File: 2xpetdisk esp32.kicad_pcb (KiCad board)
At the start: 2 copper layers, 75 x 100 mm, 252 parts, among them J1 Conn_01x08, J3 Micro_SD_Card_Det2, J31 PET_IEEE_M, J4 PET_IEEE, Q1 BSS138, Q2 BSS138, Q3 BSS138, Q4 BSS138, Q5 BSS138, U1 ESP32-WROOM-32D, U2 SN74LVC245APW, U3 AMS1117-3.3

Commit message: Added readme, images, pdf, gerber (zip).
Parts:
- added REF**: OSHW-Logo2_9.8x8mm_SilkScreen, Library:OSHW-Logo2_9.8x8mm_SilkScreen, B.Cu at (167.0, 56.5)
- added REF**: OSHW-Logo2_9.8x8mm_SilkScreen, Library:OSHW-Logo2_9.8x8mm_SilkScreen, B.Cu at (130.0, 83.5)
- J3 (x2): value Micro_SD_Card_Det2 -> Hanbo TS-013
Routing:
- net Board_1-/ports/NDAC: track 54.6 -> 64.2 mm, vias 3 -> 2
- net Board_0-/ports/NDAC: track 54.6 -> 64.2 mm, vias 3 -> 2
- net Board_1-/ports/DIO4: track 56.6 -> 55.2 mm
- net Board_0-/ports/DIO4: track 56.6 -> 55.2 mm
- net Board_0-VCC: track 154.5 -> 155.2 mm, vias 1 -> 0
- net Board_1-VCC: track 154.5 -> 155.2 mm, vias 1 -> 0
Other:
- board text added: "Based on github.com /bitfixer/petdisk-max (esp32) /svenpetersen1965/PET-IEEE-488-Extension /yo5ptd/petdisk-esp32 2025.06.27"
- board text removed: "Based on github.com/ bitfixer/petdisk-max (esp32) svenpetersen1965/PET-IEEE-488-Extension yo5ptd/petdisk esp32 2025.06.27"

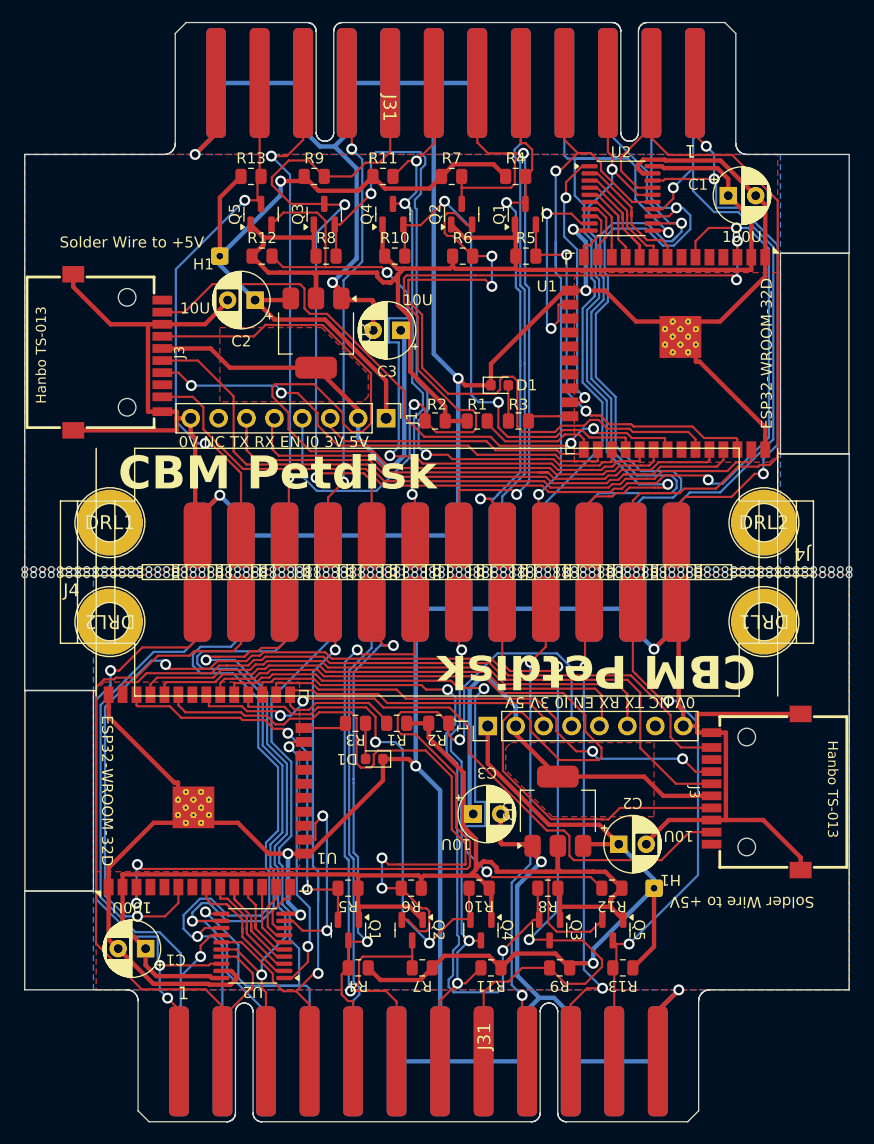
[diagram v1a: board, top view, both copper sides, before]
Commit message: Files ordered from JLCPCB.
connector silkscreen fix
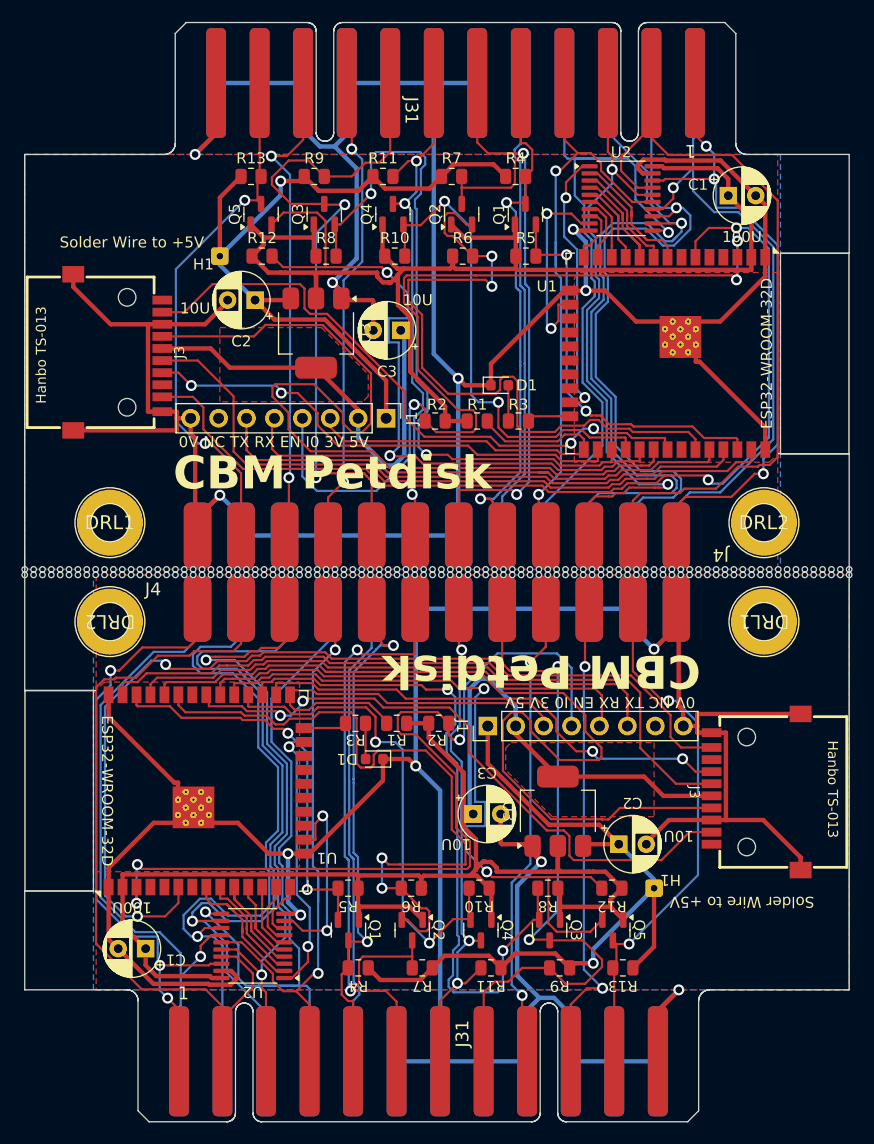
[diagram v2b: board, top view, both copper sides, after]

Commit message: Small touchup
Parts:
- removed KiKit_MB_1_1, KiKit_MB_1_64, KiKit_MB_1_65, KiKit_MB_1_66, KiKit_MB_1_67, KiKit_MB_1_68, KiKit_MB_1_69, KiKit_MB_1_70, KiKit_MB_1_71, KiKit_MB_1_72, KiKit_MB_1_73, KiKit_MB_1_74, KiKit_MB_1_75, KiKit_MB_1_76, KiKit_MB_1_77, KiKit_MB_1_78, KiKit_MB_1_79, KiKit_MB_1_80, KiKit_MB_1_81, KiKit_MB_1_82, KiKit_MB_1_83, KiKit_MB_1_84, KiKit_MB_1_85, KiKit_MB_1_86, KiKit_MB_1_87, KiKit_MB_1_88, KiKit_MB_1_89, KiKit_MB_1_90, KiKit_MB_1_91, KiKit_MB_1_92, KiKit_MB_1_93, KiKit_MB_1_94, KiKit_MB_2_64, KiKit_MB_2_65, KiKit_MB_2_66, KiKit_MB_2_67, KiKit_MB_2_68, KiKit_MB_2_69, KiKit_MB_2_70, KiKit_MB_2_71, KiKit_MB_2_72, KiKit_MB_2_73, KiKit_MB_2_74, KiKit_MB_2_75, KiKit_MB_2_76, KiKit_MB_2_77, KiKit_MB_2_78, KiKit_MB_2_79, KiKit_MB_2_80, KiKit_MB_2_81, KiKit_MB_2_82, KiKit_MB_2_83, KiKit_MB_2_84, KiKit_MB_2_85, KiKit_MB_2_86, KiKit_MB_2_87, KiKit_MB_2_88, KiKit_MB_2_89, KiKit_MB_2_90, KiKit_MB_2_91, KiKit_MB_2_92, KiKit_MB_2_93, KiKit_MB_2_94: NPTH, NPTH
- moved KiKit_MB_2_63 25.0 mm to (186.0, 70.2)
- moved KiKit_MB_2_62 24.6 mm to (184.8, 70.2)
- moved KiKit_MB_1_63 24.4 mm to (111.6, 69.8)
- moved KiKit_MB_2_61 24.2 mm to (183.6, 70.2)
- moved KiKit_MB_1_62 24.0 mm to (112.8, 69.8)
- moved KiKit_MB_2_60 23.8 mm to (182.4, 70.2)
- moved KiKit_MB_1_61 23.6 mm to (114.0, 69.8)
- moved KiKit_MB_2_59 23.4 mm to (181.2, 70.2)
- moved KiKit_MB_1_60 23.2 mm to (115.2, 69.8)
- moved KiKit_MB_2_58 23.0 mm to (180.0, 70.2)
- moved KiKit_MB_1_59 22.8 mm to (116.4, 69.8)
- moved KiKit_MB_2_57 22.6 mm to (178.7, 70.2)
- moved KiKit_MB_1_58 22.4 mm to (117.6, 69.8)
- moved KiKit_MB_2_56 22.2 mm to (177.5, 70.2)
- moved KiKit_MB_1_57 22.0 mm to (118.9, 69.8)
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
